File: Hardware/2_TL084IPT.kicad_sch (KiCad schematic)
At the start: 23 parts, among them J8 Screw_Terminal_01x08, Q4 N_Mosfet, Q5 N_Mosfet, Q6 N_Mosfet, Q7 N_Mosfet, U12 TL084

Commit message: layout part 2
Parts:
- D12, D13, D14, D15: footprint IVS_FOOTPRINTS:D_MiniMELF -> IVS_FOOTPRINTS:D_SOD323
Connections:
- net VAN5_output: now also R60.2, U12.7; no longer R59.2, U12.1
- net VAN6_output: now also R59.2, U12.1; no longer R60.2, U12.7
- net VAN7_output: now also R62.2, U12.14; no longer R61.2, U12.8
- net VAN8_output: now also R61.2, U12.8; no longer R62.2, U12.14
- net at Q4.2 (S), R51.1: now also U12.5 (+); no longer U12.3 (+)
- net at Q7.2 (S), R54.1: now also U12.10 (+); no longer U12.12 (+)
- net at Q5.2 (S), R52.1: now also U12.3 (+); no longer U12.5 (+)
- net at Q6.2 (S), R53.1: now also U12.12 (+); no longer U12.10 (+)
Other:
- moved on the sheet: C29, R59, R60, R61, R62, U12A, U12B, U12C, U12D, U12E

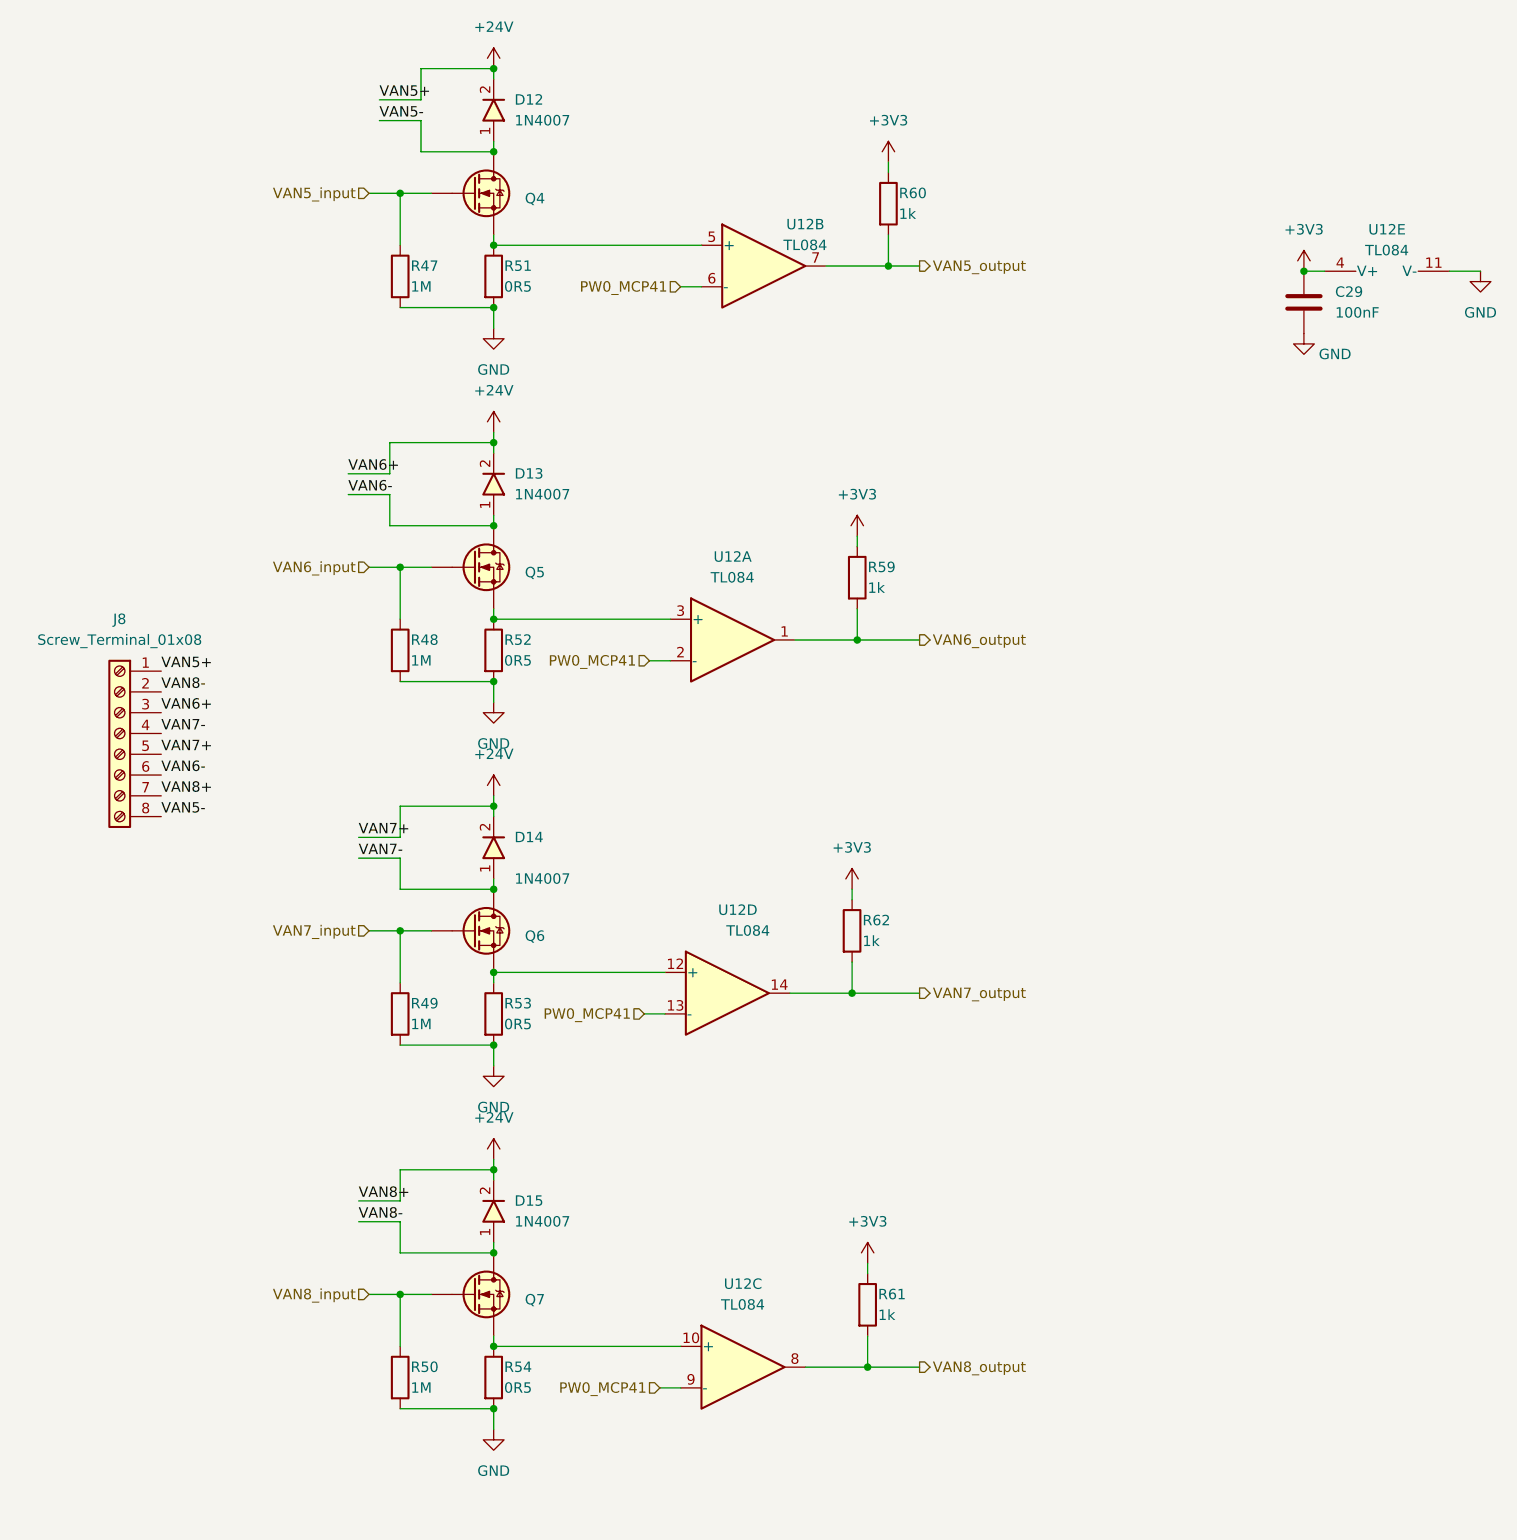
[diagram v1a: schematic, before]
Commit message: add lora, relay, opto, opamp block, led for 74595. Delete RT9193, connect boot0,1 to GND. Fix footprint crystal 8M, 74HC595, IDC pin
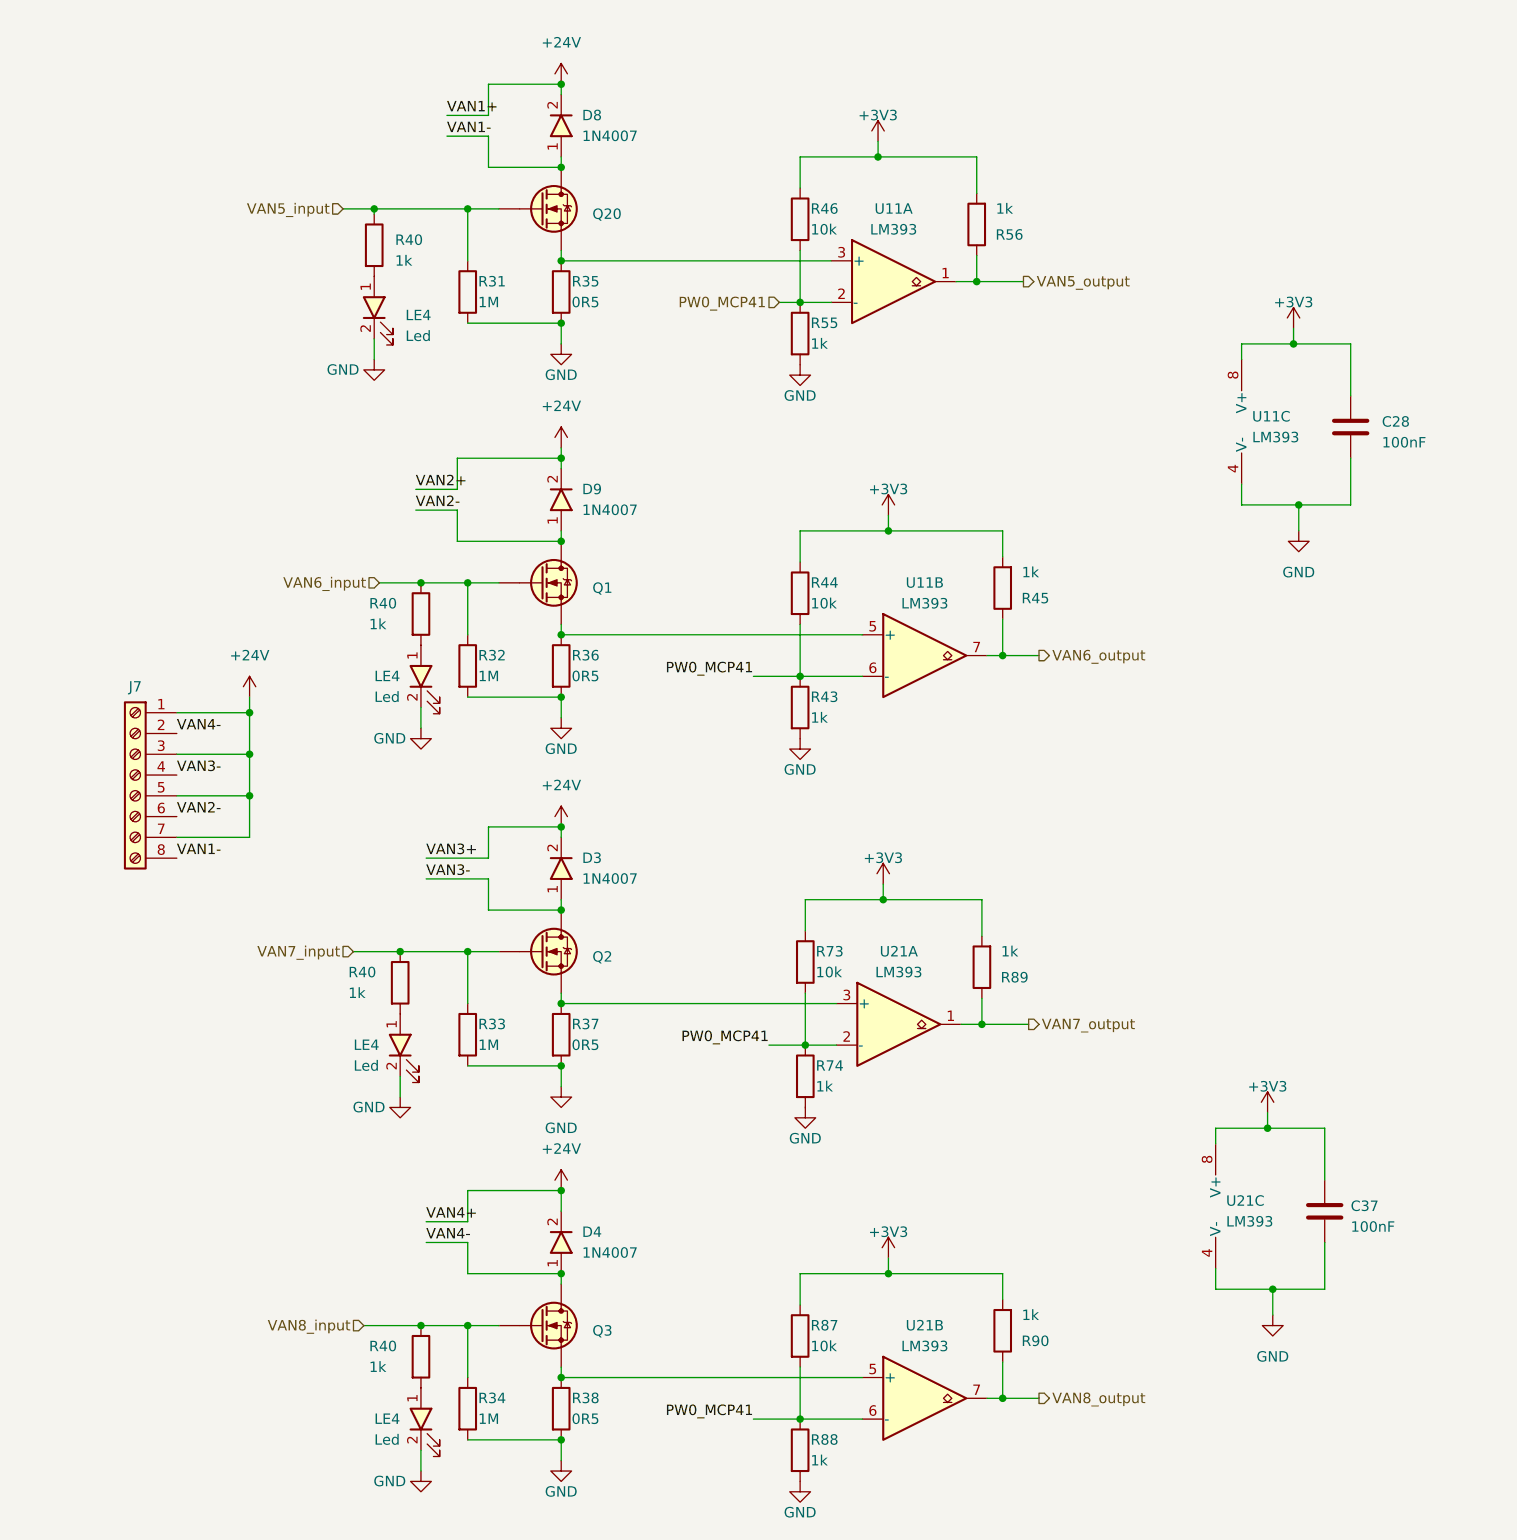
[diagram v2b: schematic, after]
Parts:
- removed C29: 100nF, IVS_FOOTPRINTS:C0603, symbol Device:C
- removed D12, D13, D14, D15: 1N4007, IVS_FOOTPRINTS:D_SOD323, symbol IVS_SYMBOL_DIR:D_Diode
- removed J8: Screw_Terminal_01x08, IVS_FOOTPRINTS:HT-3.96mm, symbol Connector:Screw_Terminal_01x08
- removed Q4, Q5, Q6, Q7: N_Mosfet, IVS_FOOTPRINTS:SOT23-3, symbol IVS_SYMBOLS:N_Mosfet
- removed R47, R48, R49, R50: 1M, IVS_FOOTPRINTS:R0603, symbol Device:R
- removed R51, R52, R53, R54: 0R5, Resistor_SMD:R_0805_2012Metric, symbol Device:R
- removed R59, R60, R61, R62: 1k, IVS_FOOTPRINTS:R0603, symbol Device:R
- removed U12: TL084, IVS_FOOTPRINTS:TSSOP14, symbol Amplifier_Operational:TL084
- added C28, C37: 100nF, IVS_FOOTPRINTS:C_0603, symbol Device:C
- added D3, D4, D8, D9: 1N4007, IVS_FOOTPRINTS:D_SOD323, symbol IVS_SYMBOL_DIR:D_Diode
- added J7: Screw_Terminal_01x08, IVS_FOOTPRINTS:HT-3.96mm, symbol Connector:Screw_Terminal_01x08
- added LE4 (x4): Led, IVS_FOOTPRINTS:LED_0603, symbol IVS_SYMBOLS:Led
- added Q1, Q2, Q20, Q3: N_Mosfet, IVS_FOOTPRINTS:SOT23-3, symbol IVS_SYMBOLS:N_Mosfet
- added R31, R32, R33, R34: 1M, IVS_FOOTPRINTS:R_0603, symbol Device:R
- added R35, R36, R37, R38: 0R5, IVS_FOOTPRINTS:R_0805, symbol Device:R
- added R40 (x4), R43, R45, R55, R56, R74, R88, R89, R90: 1k, IVS_FOOTPRINTS:R_0603, symbol Device:R
- added R44, R46, R73, R87: 10k, IVS_FOOTPRINTS:R_0603, symbol Device:R
- added U11, U21: LM393, IVS_FOOTPRINTS:SOIC-8_3.9x4.9mm_P1.27mm, symbol Comparator:LM393
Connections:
- net +24V: now also D3.2, D4.2, D8.2, D9.2, J7.1 (Pin_1), J7.3 (Pin_3), J7.5 (Pin_5), J7.7 (Pin_7)
- net +3V3: now also C28.1, C37.1, R44.1, R45.2, R46.1, R56.2, R73.1, R87.1, R89.2, R90.2, U11.8 (V+), U21.8 (V+)
- net GND: now also C28.2, C37.2, LE4.2, LE4.2, LE4.2, LE4.2, R31.2, R32.2, R33.2, R34.2, R35.2, R36.2, R37.2, R38.2, R43.2, R55.2, R74.2, R88.2, U11.4 (V-), U21.4 (V-)
- net PW0_MCP41: now also R43.1, R44.2, R46.2, R55.1, R73.2, R74.1, R87.2, R88.1, U11.2 (-), U11.6 (-), U21.2 (-), U21.6 (-)
- net VAN5_input: now also Q20.1 (G), R31.1, R40.1
- net VAN5_output: now also R56.1, U11.1
- net VAN6_input: now also Q1.1 (G), R32.1, R40.1
- net VAN6_output: now also R45.1, U11.7
- net VAN7_input: now also Q2.1 (G), R33.1, R40.1
- net VAN7_output: now also R89.1, U21.1
- net VAN8_input: now also Q3.1 (G), R34.1, R40.1
- net VAN8_output: now also R90.1, U21.7
- new net: LE4.1, R40.2 (x4)
- new net: Q20.2 (S), R35.1, U11.3 (+)
- new net: Q2.2 (S), R37.1, U21.3 (+)
- new net: Q3.2 (S), R38.1, U21.5 (+)
- new net: Q1.2 (S), R36.1, U11.5 (+)
- new net VAN1-: D8.1, J7.8 (Pin_8), Q20.3 (D)
- new net VAN2-: D9.1, J7.6 (Pin_6), Q1.3 (D)
- new net VAN3-: D3.1, J7.4 (Pin_4), Q2.3 (D)
- new net VAN4-: D4.1, J7.2 (Pin_2), Q3.3 (D)
